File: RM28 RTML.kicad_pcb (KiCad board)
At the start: 2 copper layers, 71.6 x 42.7 mm, 39 parts, among them J1 Conn_01x06_Female, J2 HV, Q1 2N7002, Q2 MCT06P10-TP, Q3 2N7002, Q4 MCT06P10-TP, U1 SPAN02A-12, U2 LM311, U3 4N35, U4 NE555

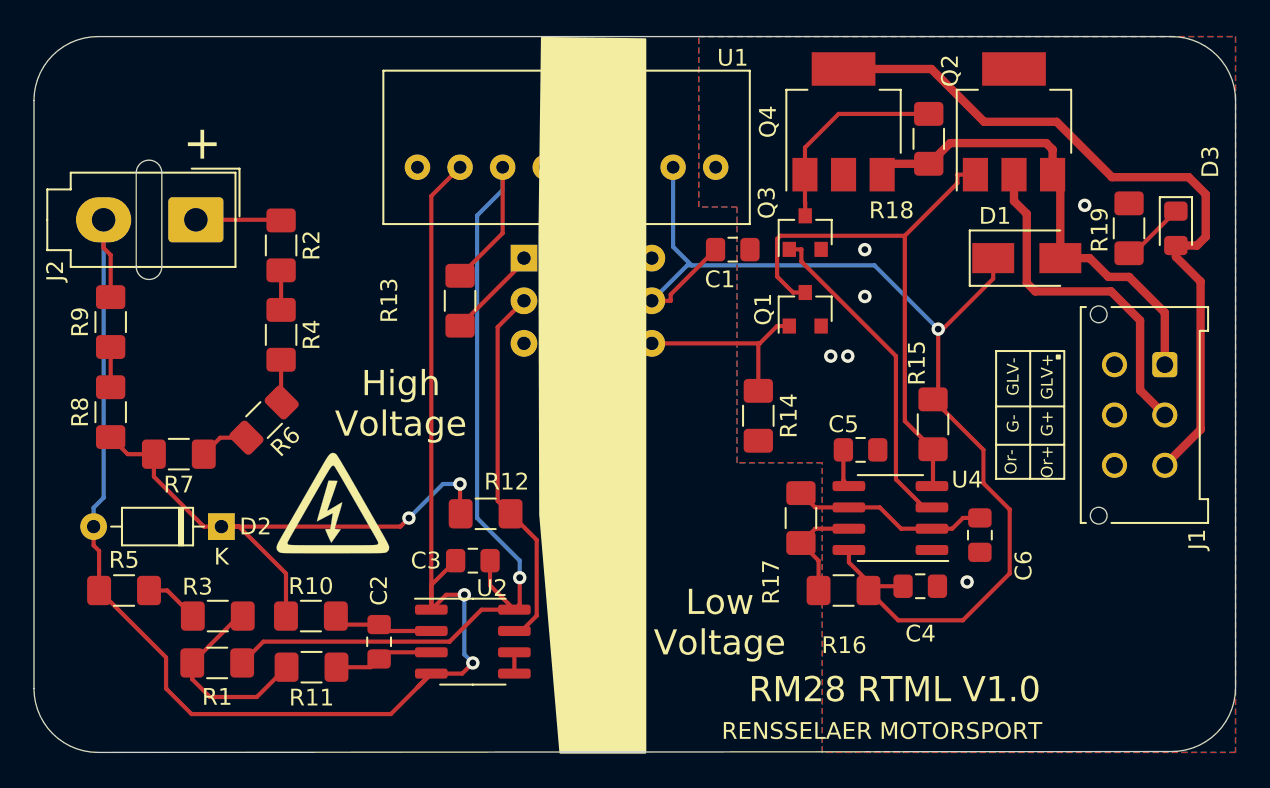
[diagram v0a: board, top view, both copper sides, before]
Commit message: Updated RTML silkscreen
Silkscreen now shows >4mm spacing
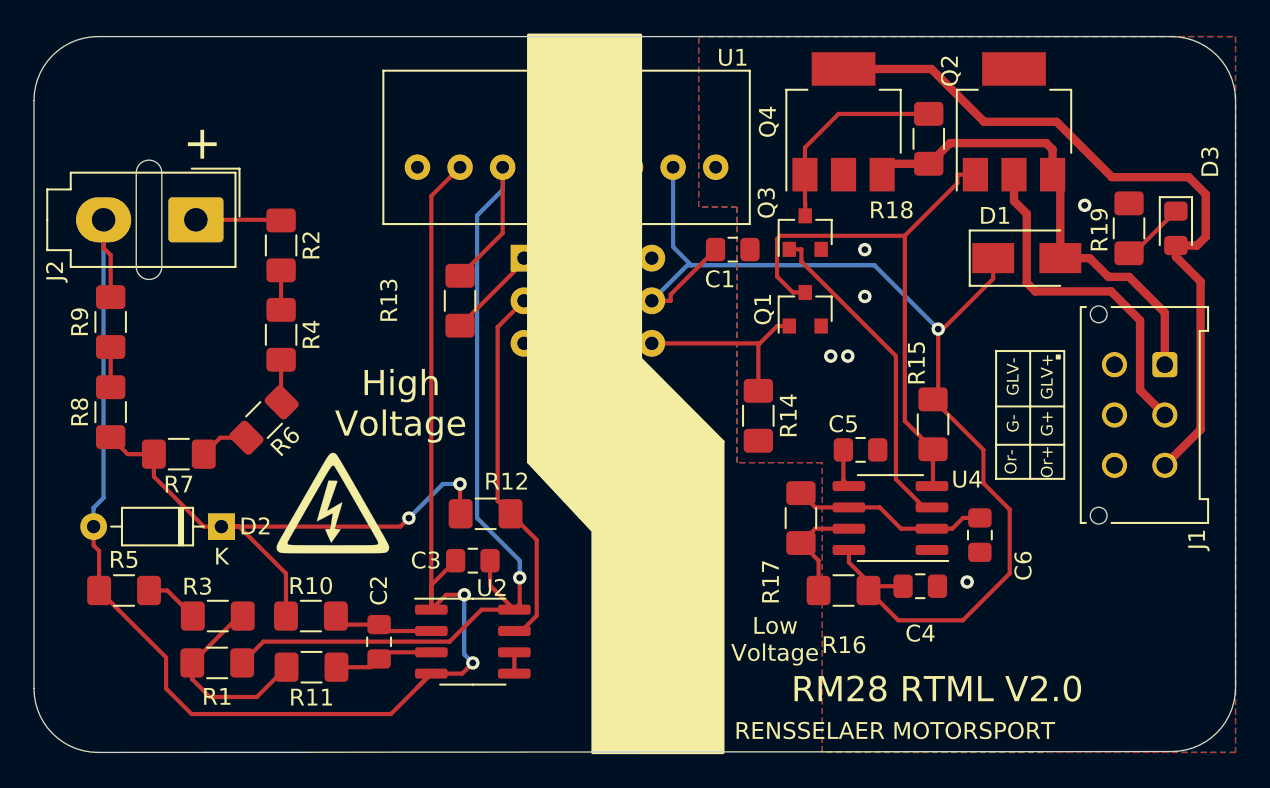
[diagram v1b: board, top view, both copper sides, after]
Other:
- board text added: "RM28 RTML V2.0"
- board text added: "[Funny Joke Here} - S.C.T."
- board text removed: "RM28 RTML V1.0"
- board text removed: "[Funny Joke Here}"
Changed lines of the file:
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@@
 		)
 		(property "Value" "4N35"
-			(at 9.398 7.41 0)
+			(at 10.26785 6.294611 0)
 			(layer "F.Fab")
 			(effects
@@
 		)
 		(property "Value" "10k"
-			(at 0 1.82 90)
+			(at -0.77298 1.926739 90)
 			(layer "F.Fab")
 			(effects
@@
 		)
 	)
+	(gr_rect
+		(start 122.939866 76.602332)
+		(end 129.647255 95.918988)
+		(stroke
+			(width 0.15)
+			(type solid)
+		)
+		(fill solid)
+		(layer "F.SilkS")
+	)
 	(gr_line
 		(start 154.8892 103.0732)
@@
 	(gr_poly
 		(pts
+			(xy 129.647255 95.918988) (xy 134.559313 100.85218) (xy 126.72554 106.117356) (xy 122.943923 102.077496)
+			(xy 122.939866 95.918988)
+		)
+		(stroke
+			(width 0.15)
+			(type solid)
+		)
+		(fill solid)
+		(layer "F.SilkS")
+	)
+	(gr_poly
+		(pts
 			(xy 154.432 95.7072) (xy 154.6352 95.7072) (xy 154.6352 95.9104) (xy 154.432 95.9104)
 		)
@@
 	)
 	(gr_line
+		(start 126.72554 106.117356)
+		(end 122.943923 102.077496)
+		(stroke
+			(width 0.15)
+			(type default)
+		)
+		(layer "F.SilkS")
+	)
+	(gr_line
+		(start 122.939866 95.918988)
+		(end 122.943923 102.077496)
+		(stroke
+			(width 0.15)
+			(type default)
+		)
+		(layer "F.SilkS")
+	)
+	(gr_line
 		(start 154.8892 95.4532)
 		(end 154.8892 103.0732)
@@
 	)
 	(gr_line
+		(start 129.647255 95.918988)
+		(end 134.559313 100.85218)
+		(stroke
+			(width 0.15)
+			(type default)
+		)
+		(layer "F.SilkS")
+	)
+	(gr_line
 		(start 152.8572 103.0732)
 		(end 152.8572 95.4532)
@@
 		(layer "F.SilkS")
 	)
+	(gr_rect
+		(start 126.775442 100.85218)
+		(end 134.559313 119.40807)
+		(stroke
+			(width 0.15)
+			(type solid)
+		)
+		(fill solid)
+		(layer "F.SilkS")
+	)
 	(gr_line
 		(start 150.8252 103.0732)
@@
 		(layer "F.SilkS")
 	)
-	(gr_poly
-		(pts
-			(xy 123.591211 88.737106) (xy 123.743982 76.775914) (xy 129.924211 76.859106) (xy 129.924211 119.404106)
-			(xy 124.844211 119.404106) (xy 123.639044 105.192957)
-		)
-		(stroke
-			(width 0.1)
-			(type solid)
-		)
-		(fill solid)
-		(layer "F.SilkS")
-	)
 	(gr_line
 		(start 150.8252 95.4532)
@@
 		(layer "Edge.Cuts")
 	)
-	(gr_text "[Funny Joke Here}\n"
-		(at 152.654 92.964 0)
+	(gr_text "[Funny Joke Here} - S.C.T.\n"
+		(at 144.317981 90.688313 0)
 		(layer "B.SilkS")
 		(effects
@@
 		)
 	)
-	(gr_text "RM28 RTML V1.0\n\n"
-		(at 144.78 116.84 0)
+	(gr_text "RM28 RTML V2.0\n\n"
+		(at 147.32 116.84 0)
 		(layer "F.SilkS")
 		(effects
@@
 	)
 	(gr_text "Low\nVoltage"
-		(at 134.354341 111.638522 0)
+		(at 137.651531 112.651524 0)
 		(layer "F.SilkS")
 		(effects
 			(font
-				(size 1.5 1.5)
+				(size 1 1)
 				(thickness 0.2)
 			)
@@
 	)
 	(gr_text "RENSSELAER MOTORSPORT"
-		(at 144.018 118.11 0)
+		(at 144.78 118.11 0)
 		(layer "F.SilkS")
 		(effects
